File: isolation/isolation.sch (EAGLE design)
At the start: 58 parts, among them IC1 XTLV61048DBVR, IC2 SN74HC14DRG3, IC3 SN74HCS32PWR, IC4 SN74HCS08DYYR, IC5 FDN359BN, IC6 FDN359BN, IC7 FDN359BN, IC8 FDN359BN, J1 S4B-XH-A_LF__SN_, J2 S4B-XH-A_LF__SN_, J3 S4B-XH-A_LF__SN_, J4 S4B-XH-A_LF__SN_, J5 S4B-XH-A_LF__SN_

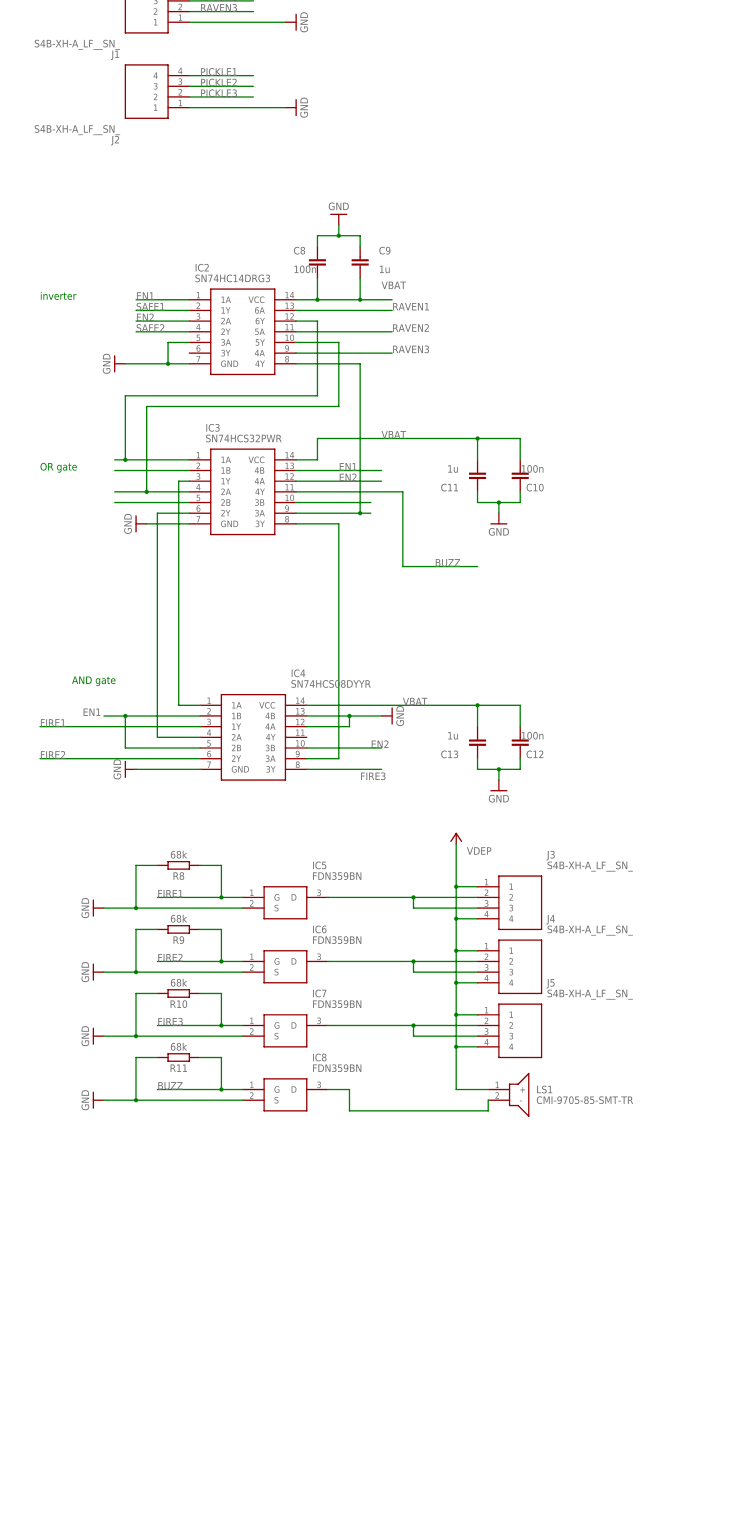
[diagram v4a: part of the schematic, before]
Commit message: indicator LEDs with manual testing
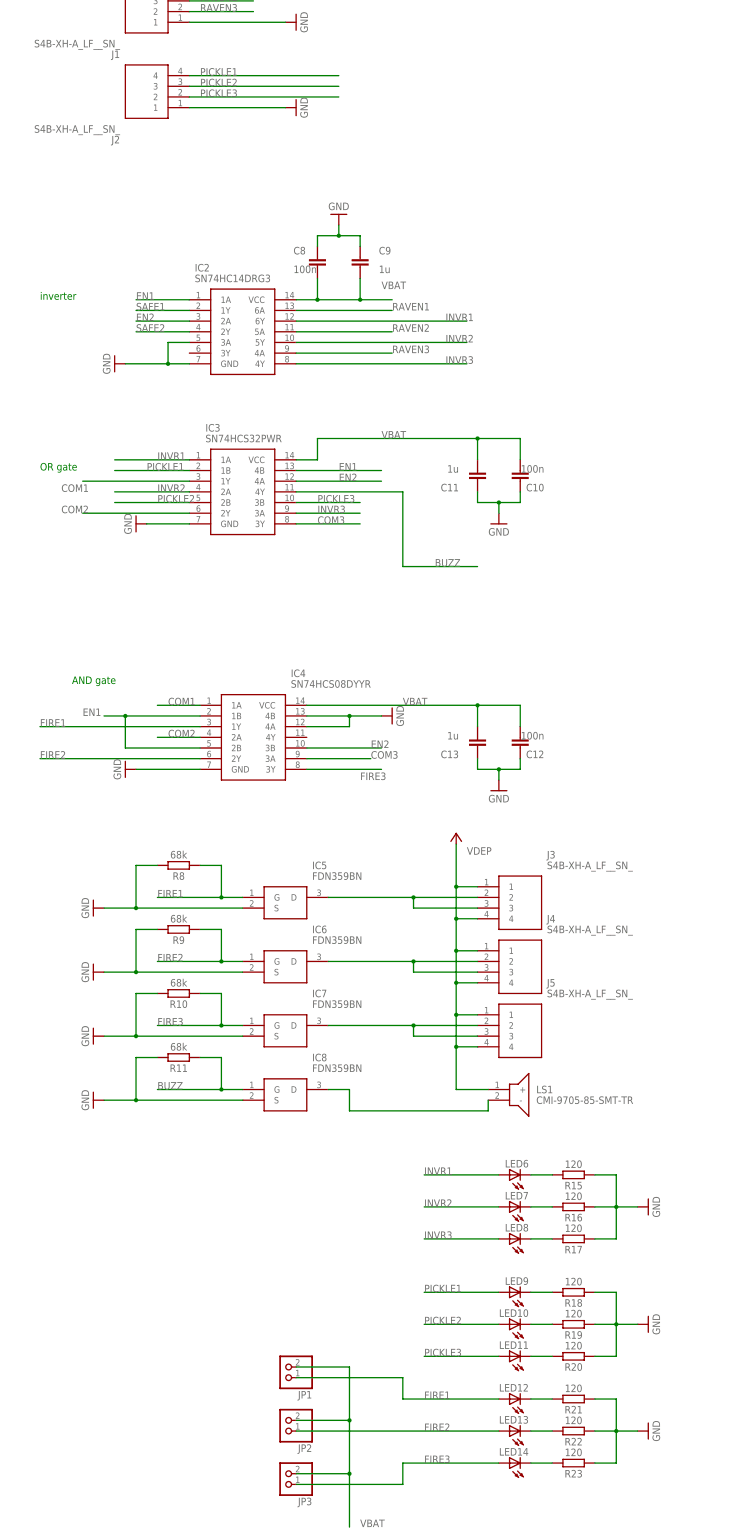
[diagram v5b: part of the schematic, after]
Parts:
- added JP1, JP2, JP3: (no value), pinhead:PINHD-1X2
- added LED10, LED11, LED12, LED13, LED14, LED6, LED7, LED8, LED9: (no value), adafruit:LEDCHIPLED_0805
- added R15, R16, R17, R18, R19, R20, R21, R22, R23: 120, Resistor:R_CHIP-0603(1608-METRIC)
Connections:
- net N$14 renamed COM3
- net N$15 renamed COM1
- net N$16 renamed COM2
- new net INVR1: IC2.6Y, IC3.1A, LED6.A
- new net INVR2: IC2.5Y, IC3.2A, LED7.A
- new net INVR3: IC2.4Y, IC3.3A, LED8.A
- new net N$18: LED7.C, R16.2
- new net N$23: LED8.C, R17.2
- new net N$27: LED6.C, R15.2
- net FIRE1: now also JP1.1, LED12.A
- net FIRE2: now also JP2.1, LED13.A
- net FIRE3: now also JP3.1, LED14.A
- net GND: now also R15.1, R16.1, R17.1, R18.1, R19.1, R20.1, R21.1, R22.1, R23.1
- net N$10: now also LED11.C, R20.2; no longer IC2.5Y, IC3.2A
- net N$11: now also LED12.C, R21.2; no longer IC3.2B
- net N$12: now also LED13.C, R22.2; no longer IC3.3B
- net N$13: now also LED14.C, R23.2; no longer IC2.4Y, IC3.3A
- net N$8: now also LED9.C, R18.2; no longer IC2.6Y, IC3.1A
- net N$9: now also LED10.C, R19.2; no longer IC3.1B
- net PICKLE1: now also IC3.1B, LED9.A
- net PICKLE2: now also IC3.2B, LED10.A
- net PICKLE3: now also IC3.3B, LED11.A
- net VBAT: now also JP1.2, JP2.2, JP3.2

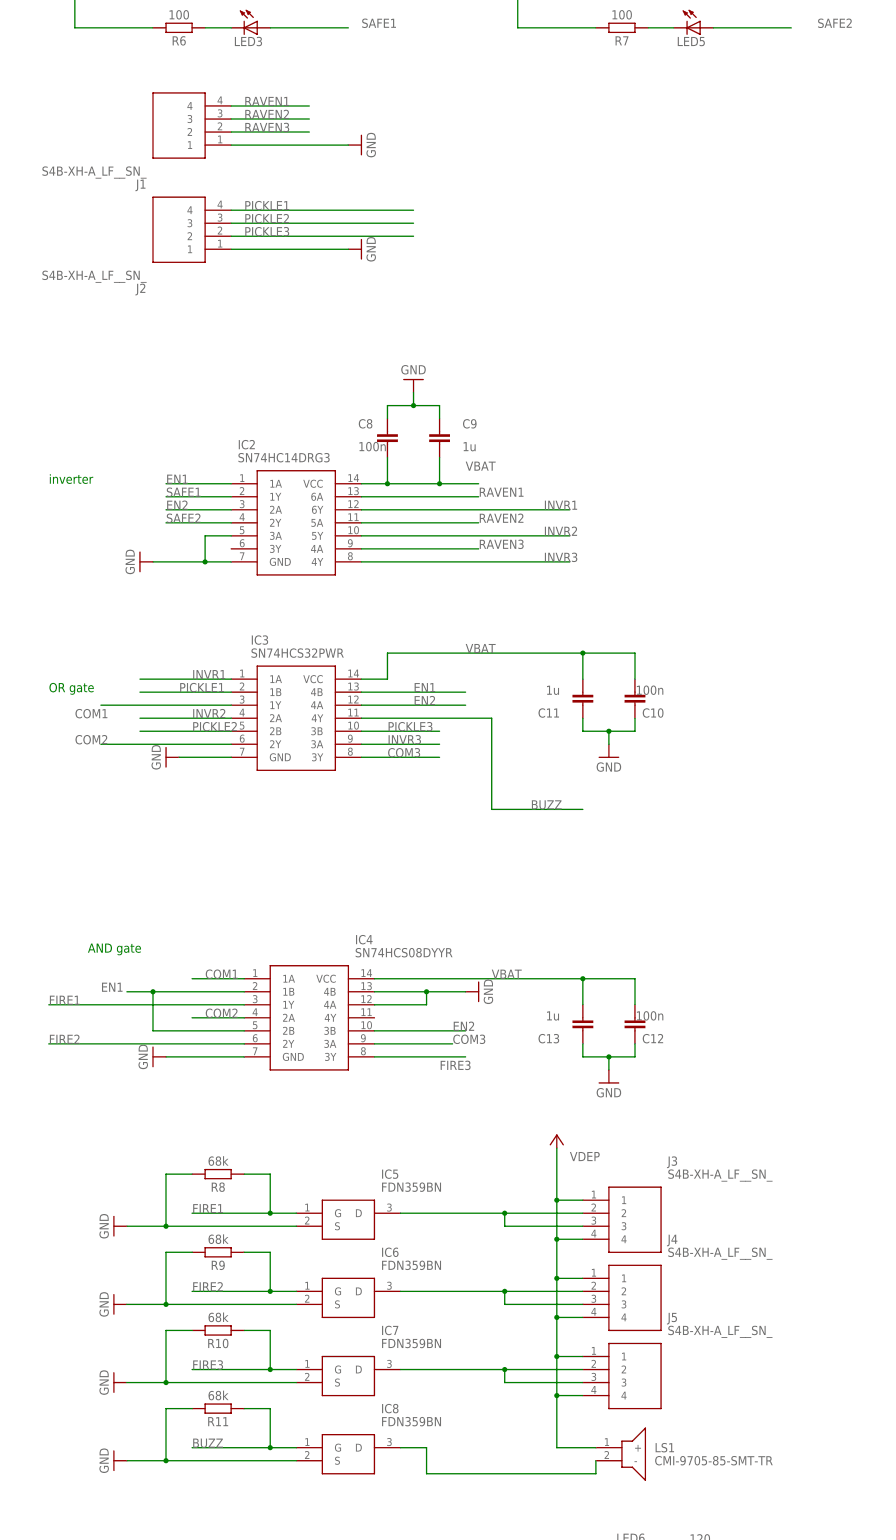
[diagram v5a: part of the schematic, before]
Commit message: switch to JST-PH
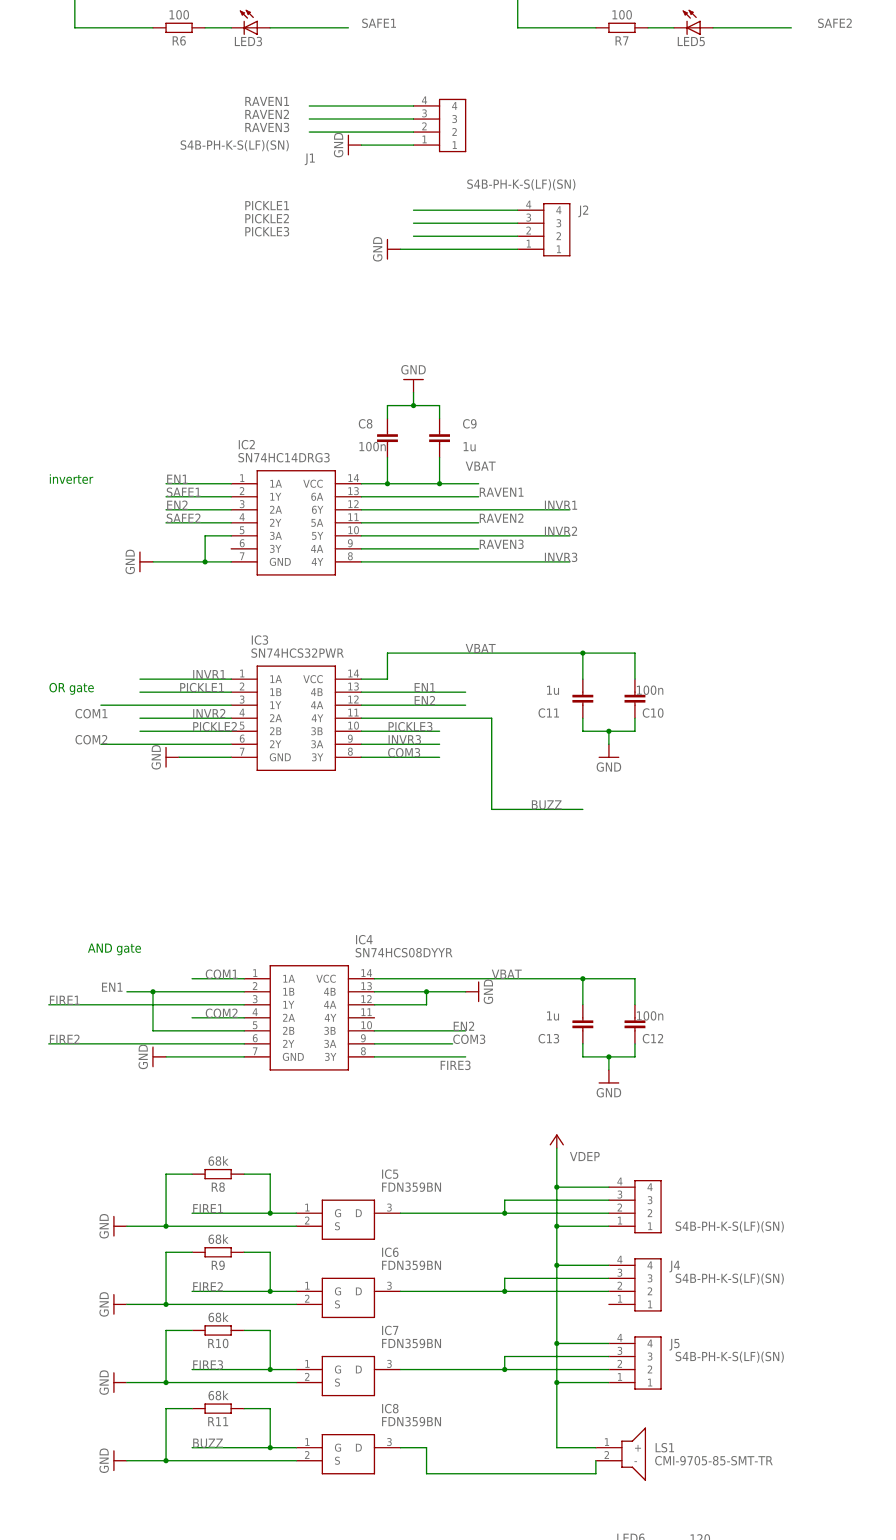
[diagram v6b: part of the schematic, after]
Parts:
- J1, J2, J3, J4, J5: value S4B-XH-A_LF__SN_ -> S4B-PH-K-S(LF)(SN); device SamacSys_Parts:S4B-XH-A_LF__SN_ -> Headers:S4B-PH-K-S(LF)(SN)
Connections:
- net VDEP: no longer J4.1
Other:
- moved on the sheet: J1, J2, J4, J5

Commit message: physically placed
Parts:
- BAT1, BAT2: value XT30UPB-M -> (none); device SamacSys_Parts:XT30UPB-M -> adafruit:JST_2PIN-THM-RA
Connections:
- net VDEP: now also J4.1
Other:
- moved on the sheet: BAT2
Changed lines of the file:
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@@
 </classes>
 <parts>
-<part name="BAT1" library="SamacSys_Parts" deviceset="XT30UPB-M" device=""/>
-<part name="BAT2" library="SamacSys_Parts" deviceset="XT30UPB-M" device=""/>
+<part name="BAT1" library="adafruit" library_urn="urn:adsk.eagle:library:420" deviceset="JST_2PIN" device="-THM-RA" package3d_urn="urn:adsk.eagle:package:6240694/1"/>
+<part name="BAT2" library="adafruit" library_urn="urn:adsk.eagle:library:420" deviceset="JST_2PIN" device="-THM-RA" package3d_urn="urn:adsk.eagle:package:6240694/1"/>
 <part name="SUPPLY1" library="Power_Symbols" library_urn="urn:adsk.eagle:library:16502351" deviceset="GND-BAR" device="" value="GND"/>
 <part name="LED1" library="adafruit" library_urn="urn:adsk.eagle:library:420" deviceset="LED" device="CHIPLED_0805" package3d_urn="urn:adsk.eagle:package:6240559/1"/>
@@
 </plain>
 <instances>
-<instance part="BAT1" gate="G$1" x="17.78" y="50.8" smashed="yes">
-<attribute name="NAME" x="34.29" y="58.42" size="1.778" layer="95" align="center-left"/>
-<attribute name="VALUE" x="34.29" y="55.88" size="1.778" layer="96" align="center-left"/>
-</instance>
-<instance part="BAT2" gate="G$1" x="17.78" y="33.02" smashed="yes">
-<attribute name="NAME" x="34.29" y="40.64" size="1.778" layer="95" align="center-left"/>
-<attribute name="VALUE" x="34.29" y="38.1" size="1.778" layer="96" align="center-left"/>
+<instance part="BAT1" gate="G$1" x="27.94" y="48.26" smashed="yes">
+<attribute name="NAME" x="31.75" y="50.8" size="1.778" layer="95" align="center-left"/>
+<attribute name="VALUE" x="44.45" y="53.34" size="1.778" layer="96" align="center-left"/>
+</instance>
+<instance part="BAT2" gate="G$1" x="27.94" y="33.02" smashed="yes">
+<attribute name="NAME" x="31.75" y="35.56" size="1.778" layer="95" align="center-left"/>
+<attribute name="VALUE" x="44.45" y="38.1" size="1.778" layer="96" align="center-left"/>
 </instance>
 <instance part="SUPPLY1" gate="G$1" x="0" y="40.64" smashed="yes" rot="R270">
@@
 <wire x1="7.62" y1="40.64" x2="7.62" y2="50.8" width="0.1524" layer="91"/>
 <pinref part="BAT1" gate="G$1" pin="1"/>
-<wire x1="7.62" y1="50.8" x2="17.78" y2="50.8" width="0.1524" layer="91"/>
+<wire x1="7.62" y1="50.8" x2="25.4" y2="50.8" width="0.1524" layer="91"/>
 <wire x1="2.54" y1="40.64" x2="7.62" y2="40.64" width="0.1524" layer="91"/>
-<wire x1="7.62" y1="40.64" x2="7.62" y2="33.02" width="0.1524" layer="91"/>
+<wire x1="7.62" y1="40.64" x2="7.62" y2="35.56" width="0.1524" layer="91"/>
 <pinref part="BAT2" gate="G$1" pin="1"/>
-<wire x1="7.62" y1="33.02" x2="17.78" y2="33.02" width="0.1524" layer="91"/>
+<wire x1="25.4" y1="35.56" x2="7.62" y2="35.56" width="0.1524" layer="91"/>
 </segment>
 <segment>
@@
 <net name="VBAT" class="0">
 <segment>
+<pinref part="BAT2" gate="G$1" pin="2"/>
+<label x="22.86" y="20.32" size="1.778" layer="95"/>
+<wire x1="15.24" y1="22.86" x2="15.24" y2="33.02" width="0.1524" layer="91"/>
 <pinref part="BAT1" gate="G$1" pin="2"/>
-<wire x1="17.78" y1="48.26" x2="15.24" y2="48.26" width="0.1524" layer="91"/>
-<wire x1="15.24" y1="48.26" x2="15.24" y2="30.48" width="0.1524" layer="91"/>
-<pinref part="BAT2" gate="G$1" pin="2"/>
-<wire x1="15.24" y1="30.48" x2="17.78" y2="30.48" width="0.1524" layer="91"/>
-<wire x1="15.24" y1="30.48" x2="15.24" y2="22.86" width="0.1524" layer="91"/>
-<junction x="15.24" y="30.48"/>
-<label x="22.86" y="20.32" size="1.778" layer="95"/>
+<wire x1="15.24" y1="33.02" x2="15.24" y2="48.26" width="0.1524" layer="91"/>
+<wire x1="15.24" y1="48.26" x2="25.4" y2="48.26" width="0.1524" layer="91"/>
+<wire x1="25.4" y1="33.02" x2="15.24" y2="33.02" width="0.1524" layer="91"/>
+<junction x="15.24" y="33.02"/>
 </segment>
 <segment>
@@
 <pinref part="J3" gate="G$1" pin="4"/>
 <wire x1="86.36" y1="-325.12" x2="86.36" y2="-317.5" width="0.1524" layer="91"/>
-<wire x1="86.36" y1="-317.5" x2="86.36" y2="-302.26" width="0.1524" layer="91"/>
+<wire x1="86.36" y1="-317.5" x2="86.36" y2="-309.88" width="0.1524" layer="91"/>
+<wire x1="86.36" y1="-309.88" x2="86.36" y2="-302.26" width="0.1524" layer="91"/>
 <wire x1="86.36" y1="-302.26" x2="86.36" y2="-294.64" width="0.1524" layer="91"/>
 <wire x1="86.36" y1="-294.64" x2="86.36" y2="-287.02" width="0.1524" layer="91"/>
@@
 <junction x="86.36" y="-325.12"/>
 <label x="88.9" y="-281.94" size="1.778" layer="95"/>
+<pinref part="J4" gate="G$1" pin="1"/>
+<wire x1="96.52" y1="-309.88" x2="86.36" y2="-309.88" width="0.1524" layer="91"/>
+<junction x="86.36" y="-309.88"/>
 </segment>
 </net>

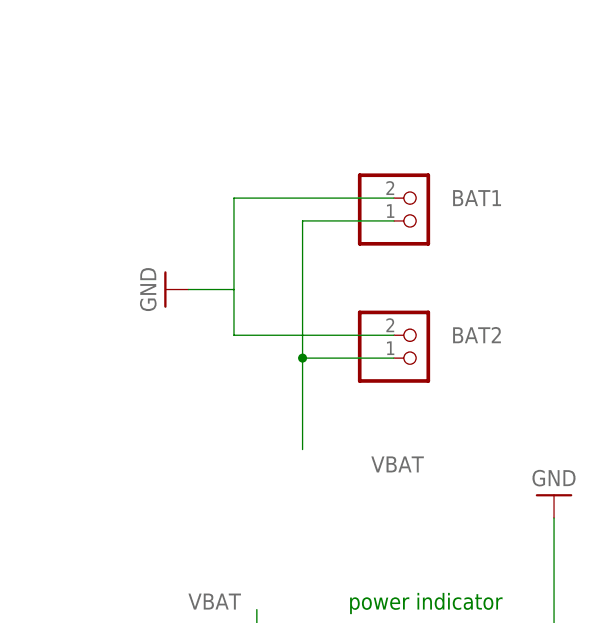
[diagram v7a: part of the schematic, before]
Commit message: pads for ext power in
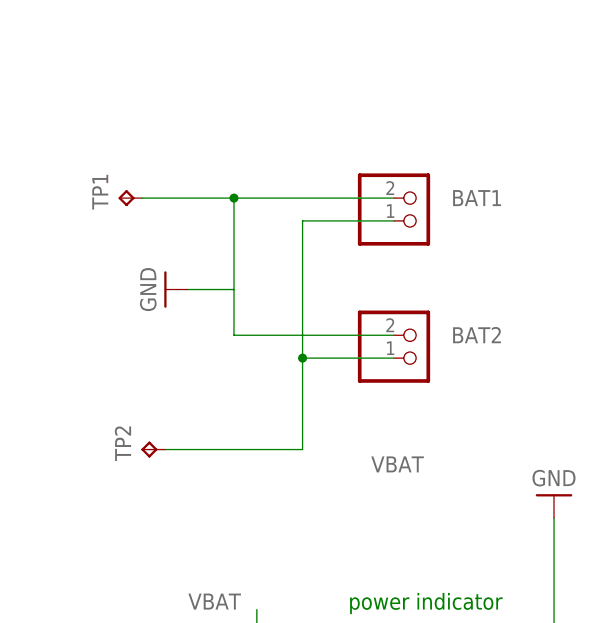
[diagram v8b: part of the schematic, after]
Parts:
- added TP1, TP2: TPPAD1-20Y, testpad:TPPAD1-20Y
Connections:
- net GND: now also TP1.TP
- net VBAT: now also TP2.TP
